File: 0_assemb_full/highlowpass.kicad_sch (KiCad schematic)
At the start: 53 parts, among them U1 X-opamp,IEEE, U10 X-opamp,IEEE, U11 X-opamp,IEEE, U12 X-opamp,IEEE, U13 X-opamp,IEEE, U14 X-opamp,IEEE, U2 X-opamp,IEEE, U3 X-opamp,IEEE, U4 X-opamp,IEEE, U5 X-opamp,IEEE, U6 X-opamp,IEEE, U7 X-opamp,IEEE, U8 X-opamp,IEEE, U9 X-opamp,IEEE

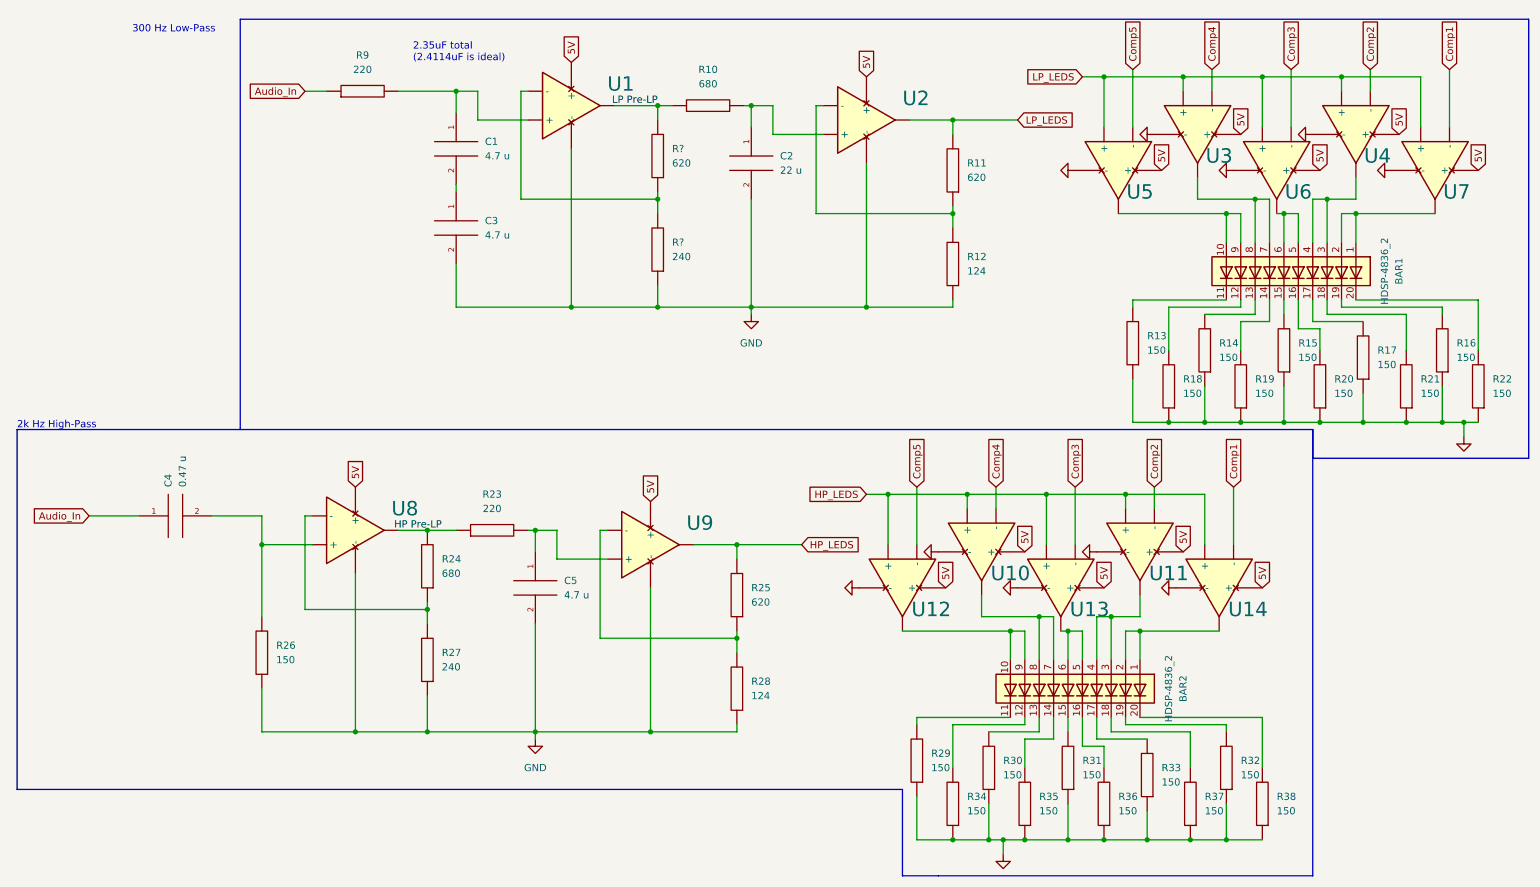
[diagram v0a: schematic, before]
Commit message: Added the full schematic file and included the filters
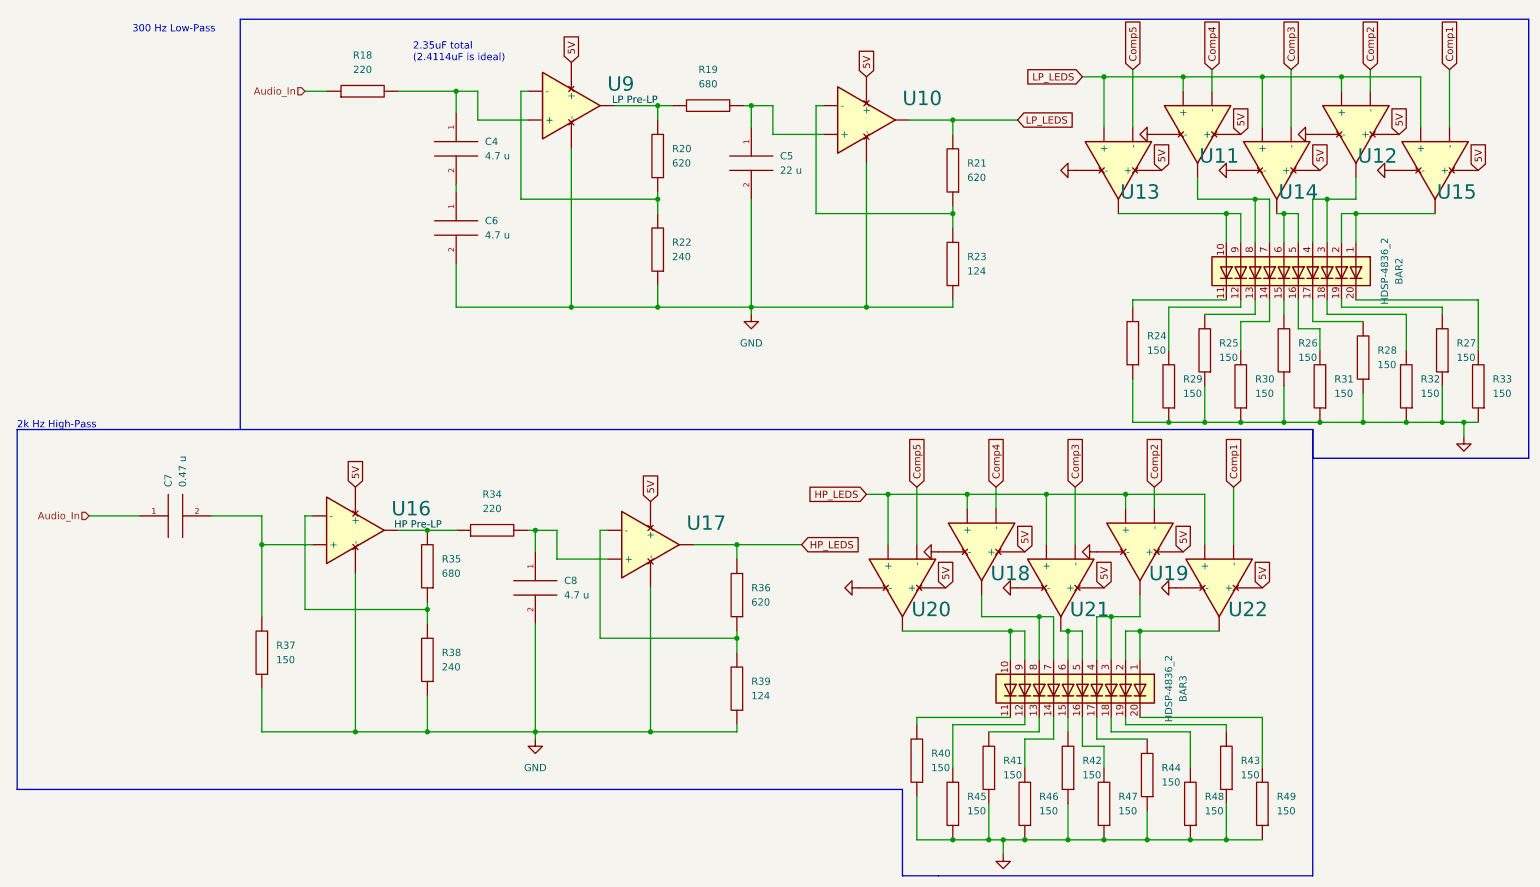
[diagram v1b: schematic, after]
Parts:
- gave numbers to parts that had none: 2
- renumbered BAR1 to BAR2, BAR2 to BAR3, C1 to C4, C2 to C5, C3 to C6, C4 to C7, C5 to C8, R9 to R18, R10 to R19, R11 to R21, R12 to R23, R13 to R24, R14 to R25, R15 to R26, R16 to R27, R17 to R28, R18 to R29, R19 to R30, R20 to R31, R21 to R32, R22 to R33, R23 to R34, R24 to R35, R25 to R36, R26 to R37, R27 to R38, R28 to R39, R29 to R40, R30 to R41, R31 to R42, R32 to R43, R33 to R44, R34 to R45, R35 to R46, R36 to R47, R37 to R48, R38 to R49, U2 to U10, U3 to U11, U4 to U12, U5 to U13, U6 to U14, U7 to U15, U8 to U16, U9 to U17, U10 to U18, U11 to U19, U12 to U20, U13 to U21, U14 to U22, U1 to U9

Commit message: Added STM32F091RCTx symbol and power symbols
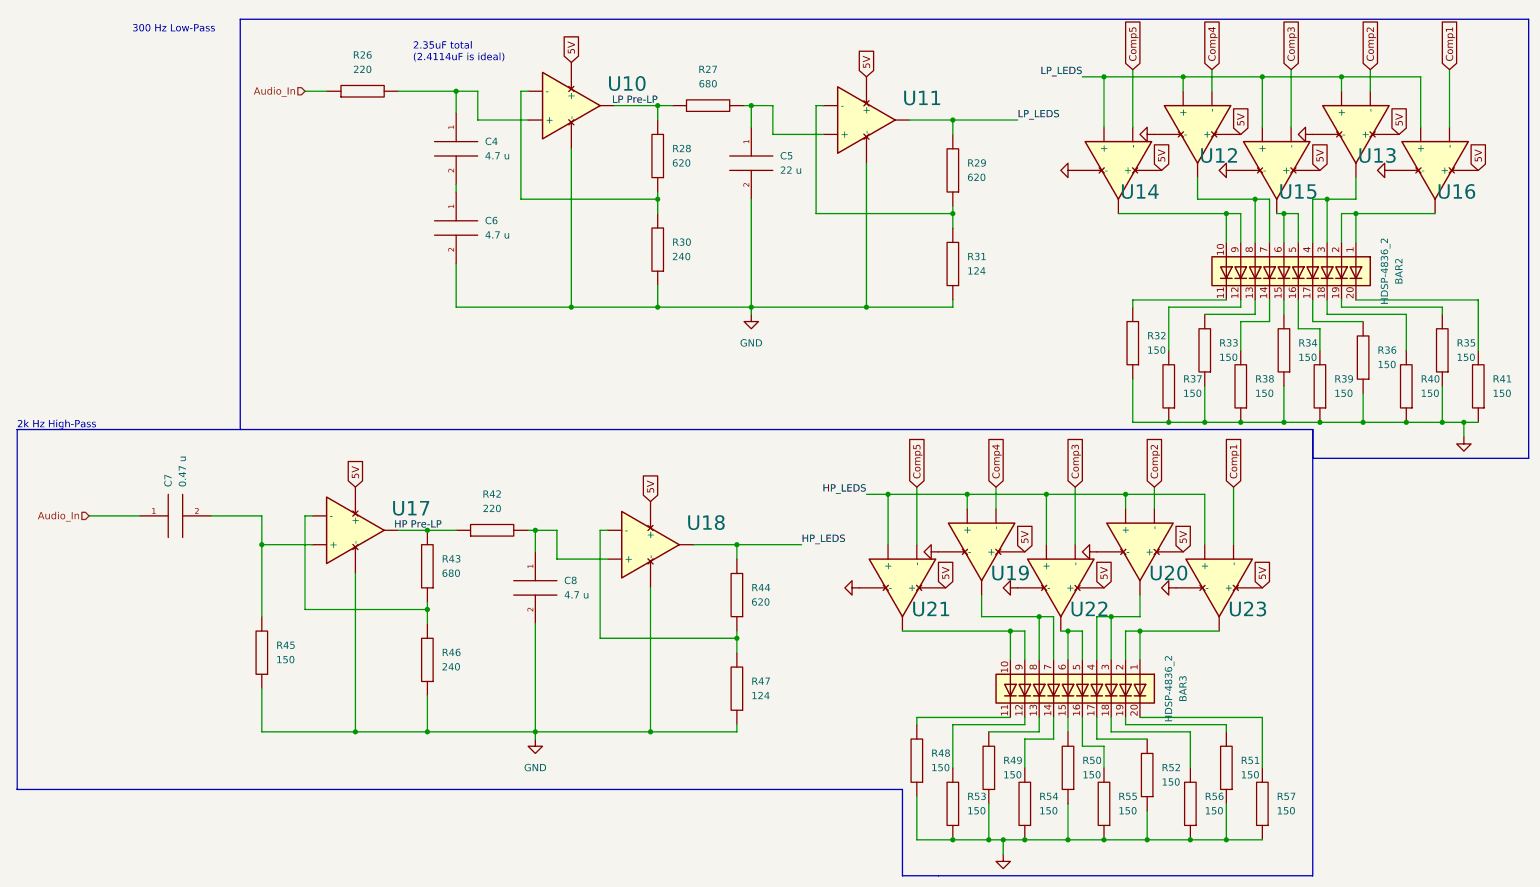
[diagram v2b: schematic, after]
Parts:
- renumbered R18 to R26, R19 to R27, R20 to R28, R21 to R29, R22 to R30, R23 to R31, R24 to R32, R25 to R33, R26 to R34, R27 to R35, R28 to R36, R29 to R37, R30 to R38, R31 to R39, R32 to R40, R33 to R41, R34 to R42, R35 to R43, R36 to R44, R37 to R45, R38 to R46, R39 to R47, R40 to R48, R41 to R49, R42 to R50, R43 to R51, R44 to R52, R45 to R53, R46 to R54, R47 to R55, R48 to R56, R49 to R57, U9 to U10, U10 to U11, U11 to U12, U12 to U13, U13 to U14, U14 to U15, U15 to U16, U16 to U17, U17 to U18, U18 to U19, U19 to U20, U20 to U21, U21 to U22, U22 to U23

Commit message: Additional changes
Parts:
- added RV4, RV6: 1K, symbol Device:Varistor_US
- added RV5: 10K, symbol Device:Varistor_US
- added RV7: 680, symbol Device:Varistor_US
- C10: renamed from C8; value 4.7 u -> 4.7u
- C6: renamed from C4; value 4.7 u -> 4.7u
- C7: renamed from C5; value 22 u -> 22u
- C8: renamed from C6; value 4.7 u -> 4.7u
- C9: renamed from C7; value 0.47 u -> 0.47u
- R26, R42: value 220 -> 470; symbol pspice:R -> Device:R_US
- R27: value 680 -> 4.7K; symbol pspice:R -> Device:R_US
- R28, R29, R30, R31, R32, R33, R34, R35, R36, R37, R38, R39, R40, R41, R43, R44, R46, R47, R48, R49, R50, R51, R52, R53, R54, R55, R56, R57: symbol pspice:R -> Device:R_US
- R45: value 150 -> 330; symbol pspice:R -> Device:R_US
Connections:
- net Audio_In: now also RV4.2
- net GND: now also RV7.2
- net HP Pre-LP: now also RV6.2
- net LP Pre-LP: now also RV5.2
- net at C7.1, R27.2, U11.1 (+): now also RV5.1
- net at C9.2, R45.2, U17.1 (+): now also RV7.1
- net at C6.1, R26.2, U10.1 (+): now also RV4.1
- net at C10.1, R42.2, U18.1 (+): now also RV6.1
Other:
- note added: "Ideal: 150 Ohms"
- note added: "Ideal: 220 Ohms"
- note added: "Ideal: 680 Ohms"

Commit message: Removed varistors, updated some STM32 connections
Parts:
- removed RV4, RV6: 1K, symbol Device:Varistor_US
- removed RV5: 10K, symbol Device:Varistor_US
- removed RV7: 680, symbol Device:Varistor_US
- R26, R42: value 470 -> 220
- R27: value 4.7K -> 680
- R45: value 330 -> 150
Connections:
- net at R26.2, U10.1 (+): no longer C6.1
- net at R42.2, U18.1 (+): no longer C10.1
- net HP_LEDS renamed ADC_HP
- net LP_LEDS renamed ADC_LP
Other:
- note removed: "Ideal: 150 Ohms"
- note removed: "Ideal: 220 Ohms"
- note removed: "Ideal: 680 Ohms"

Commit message: Bandpass filter all set now!
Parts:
- renumbered C8 to C10, C9 to C11, C10 to C12, C6 to C8, C7 to C9, R26 to R30, R27 to R31, R28 to R32, R29 to R33, R30 to R34, R31 to R35, R32 to R36, R33 to R37, R34 to R38, R35 to R39, R36 to R40, R37 to R41, R38 to R42, R39 to R43, R40 to R44, R41 to R45, R42 to R46, R43 to R47, R44 to R48, R45 to R49, R46 to R50, R47 to R51, R48 to R52, R49 to R53, R50 to R54, R51 to R55, R52 to R56, R53 to R57, R54 to R58, R55 to R59, R56 to R60, R57 to R61, U10 to U11, U11 to U12, U12 to U13, U13 to U14, U14 to U15, U15 to U16, U16 to U17, U17 to U18, U18 to U19, U19 to U20, U20 to U21, U21 to U22, U22 to U23, U23 to U24

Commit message: A bunch of changes to the schematics
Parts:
- removed BAR2, BAR3: HDSP-4836_2, Display:HDSP-4836, symbol LED:HDSP-4836_2
- removed R36, R37, R38, R39, R40, R41, R42, R43, R44, R45, R52, R53, R54, R55, R56, R57, R58, R59, R60, R61: 150, symbol Device:R_US
- removed U13, U14, U15, U16, U17, U20, U21, U22, U23, U24: X-opamp,IEEE, symbol Generic:X-opamp,IEEE

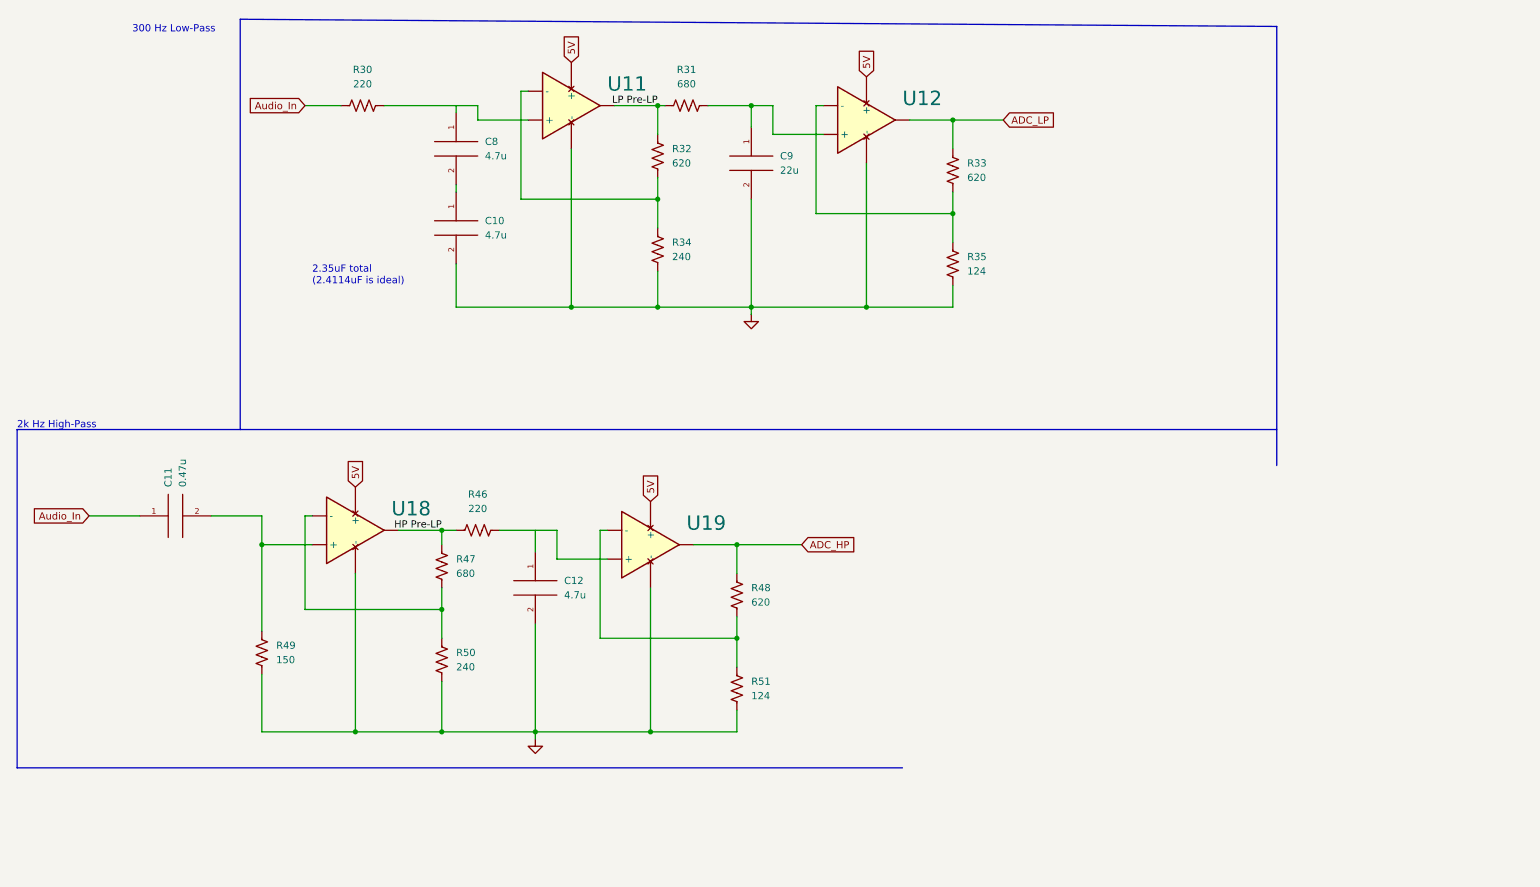
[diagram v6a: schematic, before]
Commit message: Updates to the filter system
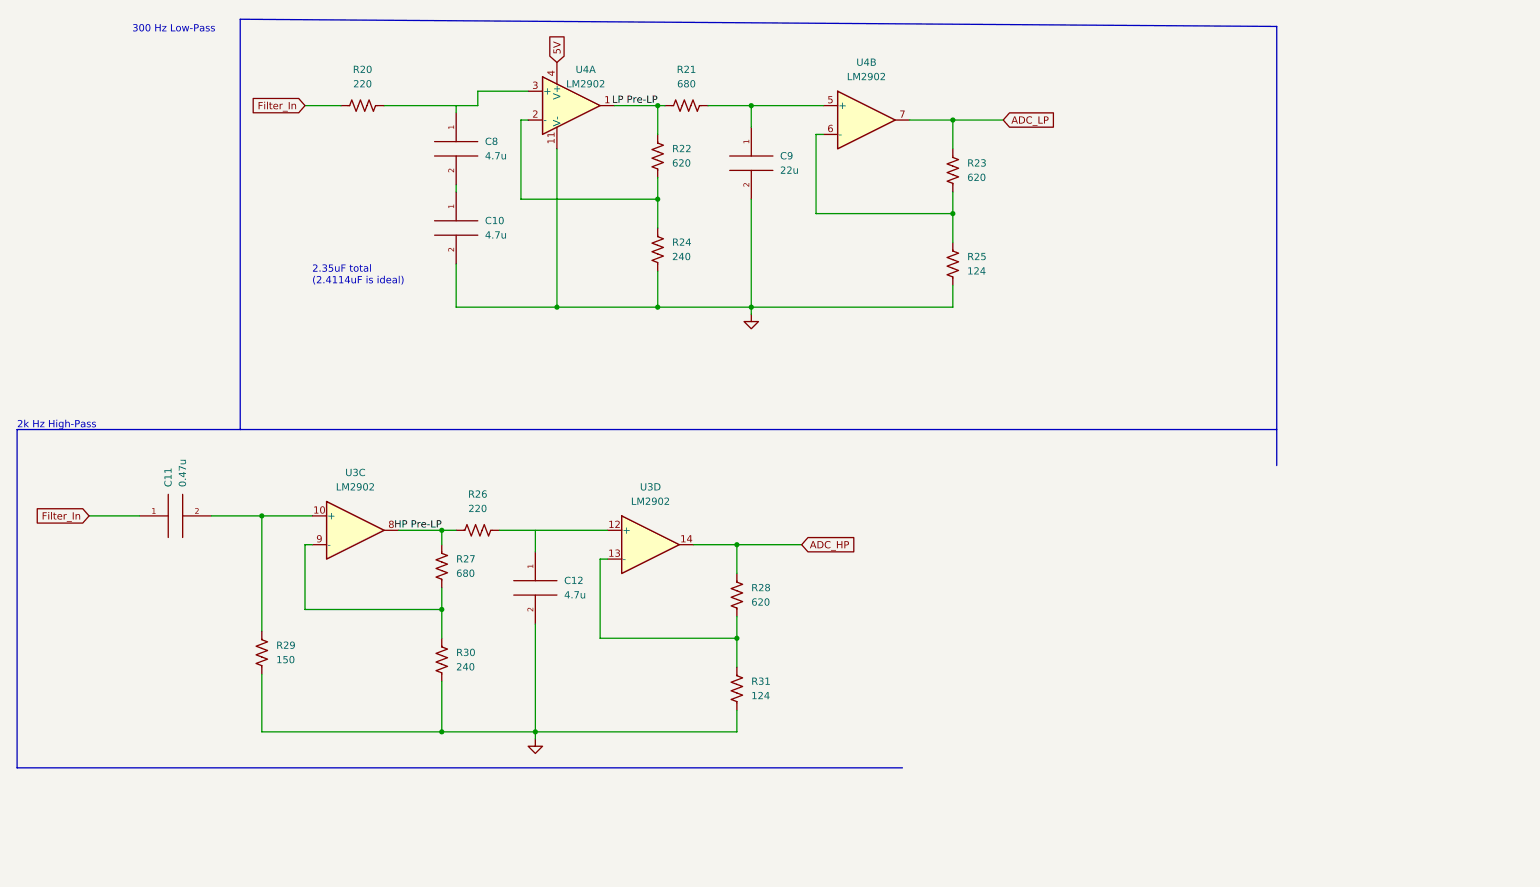
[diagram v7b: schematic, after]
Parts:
- removed U11, U12, U18, U19: X-opamp,IEEE, symbol Generic:X-opamp,IEEE
- added U3, U4: LM2902, symbol Amplifier_Operational:LM2902
- renumbered R30 to R20, R31 to R21, R32 to R22, R33 to R23, R34 to R24, R35 to R25, R46 to R26, R47 to R27, R48 to R28, R49 to R29, R50 to R30, R51 to R31
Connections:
- net 5V: now also U4.4 (V+)
- net ADC_HP: now also U3.14
- net ADC_LP: now also U4.7
- net GND: now also U4.11 (V-)
- net HP Pre-LP: now also U3.8
- net LP Pre-LP: now also U4.1
- net at R22.1, R24.2: now also U4.2 (-)
- net at C9.1, R21.2: now also U4.5 (+)
- net at C11.2, R29.2: now also U3.10 (+)
- net at R23.1, R25.2: now also U4.6 (-)
- net at R28.1, R31.2: now also U3.13 (-)
- net at R27.1, R30.2: now also U3.9 (-)
- net at R20.2: now also U4.3 (+)
- net at R26.2: now also U3.12 (+)
- net Audio_In renamed Filter_In

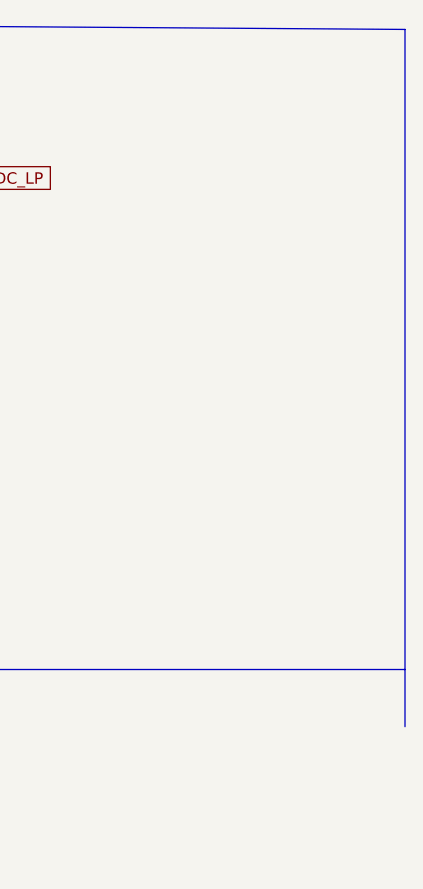
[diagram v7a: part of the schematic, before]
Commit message: Added amplifier circuit and the programming header.
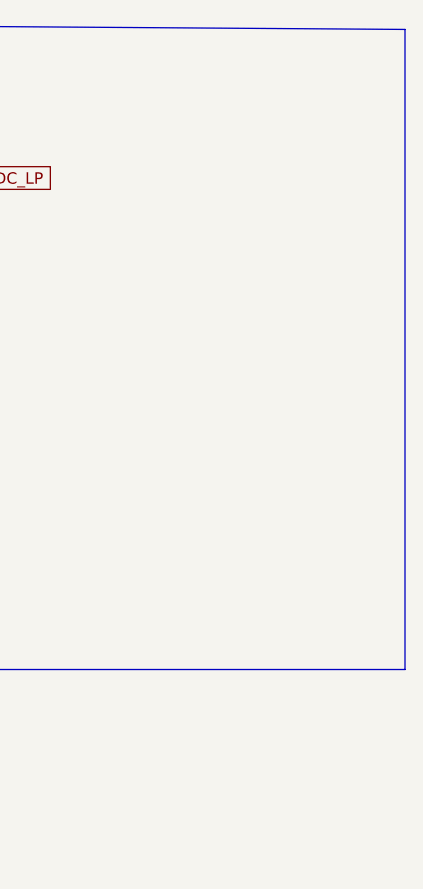
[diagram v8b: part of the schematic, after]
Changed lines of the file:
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@@
     (stroke (width 0) (type default) (color 0 0 0 0))
   )
-  (polyline (pts (xy 236.22 92.71) (xy 236.22 15.24))
+  (polyline (pts (xy 236.22 86.36) (xy 236.22 15.24))
     (stroke (width 0) (type default) (color 0 0 0 0))
   )
@@
   (symbol (lib_id "power:GND") (at 143.51 66.04 0) (unit 1)
     (in_bom yes) (on_board yes) (fields_autoplaced)
-    (property "Reference" "#PWR08" (id 0) (at 143.51 72.39 0)
+    (property "Reference" "#PWR014" (id 0) (at 143.51 72.39 0)
       (effects (font (size 1.27 1.27)) hide)
     )
@@
   (symbol (lib_id "power:GND") (at 105.41 140.97 0) (unit 1)
     (in_bom yes) (on_board yes) (fields_autoplaced)
-    (property "Reference" "#PWR09" (id 0) (at 105.41 147.32 0)
-      (effects (font (size 1.27 1.27)) hide)
-    )
+    (property "Reference" "#PWR015" (id 0) (at 105.41 147.32 0)
+      (effects (font (size 1.27 1.27)) hide)
+    )
